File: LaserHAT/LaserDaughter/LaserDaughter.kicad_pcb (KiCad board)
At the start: 2 copper layers, 26.5 x 23.5 mm, 28 parts, among them J1 HAT_J8, J2 Conn_02x02_Counter_Clockwise, J3 HAT_J9, J4 PD_K-LASER_V (solder jumper), J5 RED_SHUNT, Q1 AO9926B, Q2 NDT3055L, SW5 PCM12SMTR, U2 MT3608, U3 TLV2371DBV

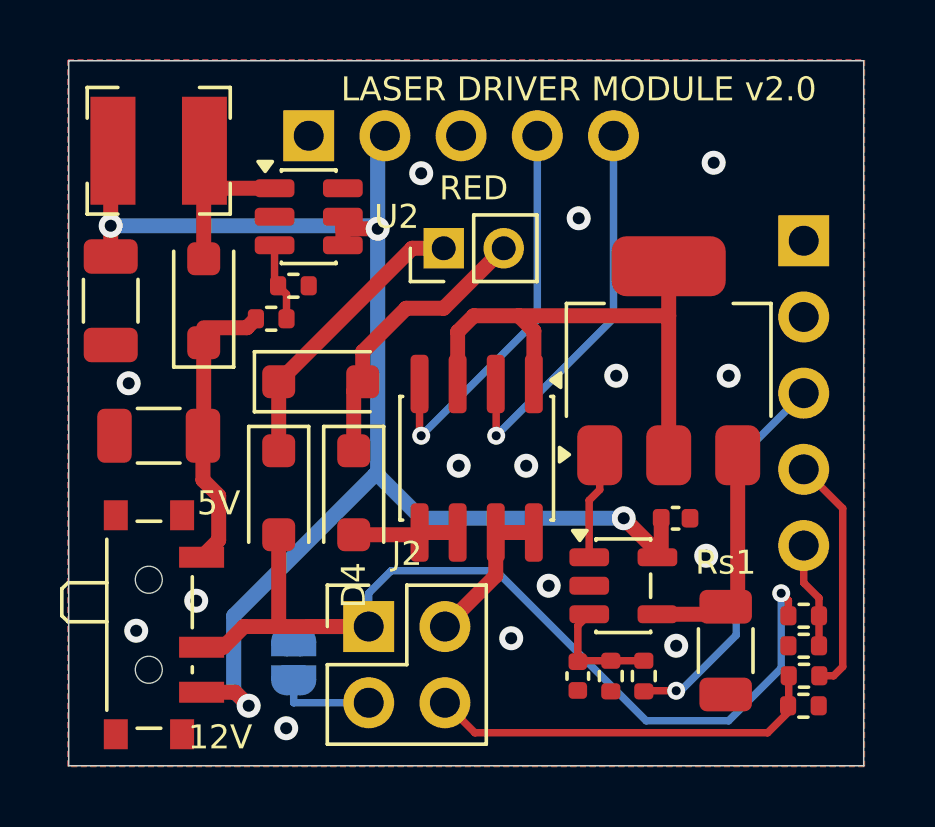
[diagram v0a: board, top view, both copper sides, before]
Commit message: Edited silk screen in EStim daughterboard
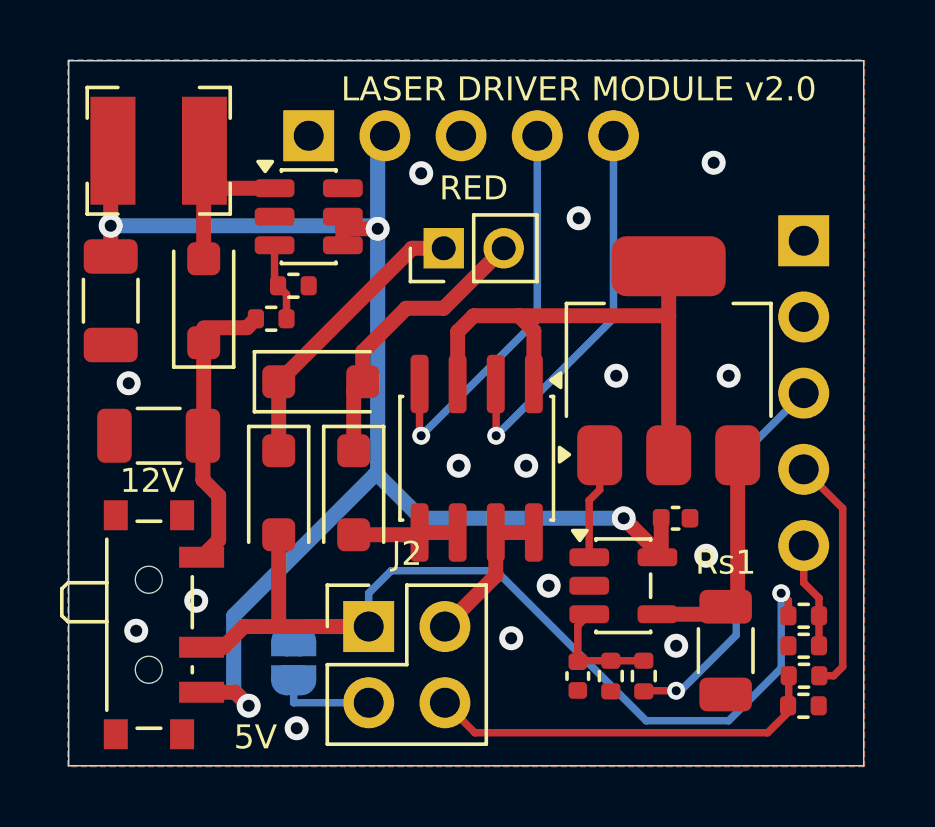
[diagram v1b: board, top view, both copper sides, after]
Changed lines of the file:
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@@
 			(at 3.083571 0 90)
 			(layer "F.SilkS")
+			(hide yes)
 			(effects
 				(font
@@
 			(at 2.933571 0 0)
 			(layer "F.SilkS")
+			(hide yes)
 			(effects
 				(font
@@
 		(layer "Edge.Cuts")
 	)
-	(gr_text "5V"
-		(at 106 90.75 0)
+	(gr_text "12V"
+		(at 102.7 90 0)
 		(layer "F.SilkS")
 		(effects
@@
 				(thickness 0.12)
 			)
+			(justify left)
 		)
 	)
-	(gr_text "12V"
-		(at 106.05 98.55 0)
+	(gr_text "5V"
+		(at 106.5 98.55 0)
 		(layer "F.SilkS")
 		(effects
@@
 				(thickness 0.12)
 			)
+			(justify left)
 		)
 	)
@@
 	)
 	(via
-		(at 108.25 98.25)
+		(at 108.6 98.25)
 		(size 0.8)
 		(drill 0.4)
